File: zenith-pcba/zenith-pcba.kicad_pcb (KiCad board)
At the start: 2 copper layers, 20 parts, among them SW1 G4R152312, U1 XC7A50T-CSG325, U2 K4B4G1646E-BCNB, U3 CH347T, U4 AP63203WU, X1 SX5B8.000F1520F30

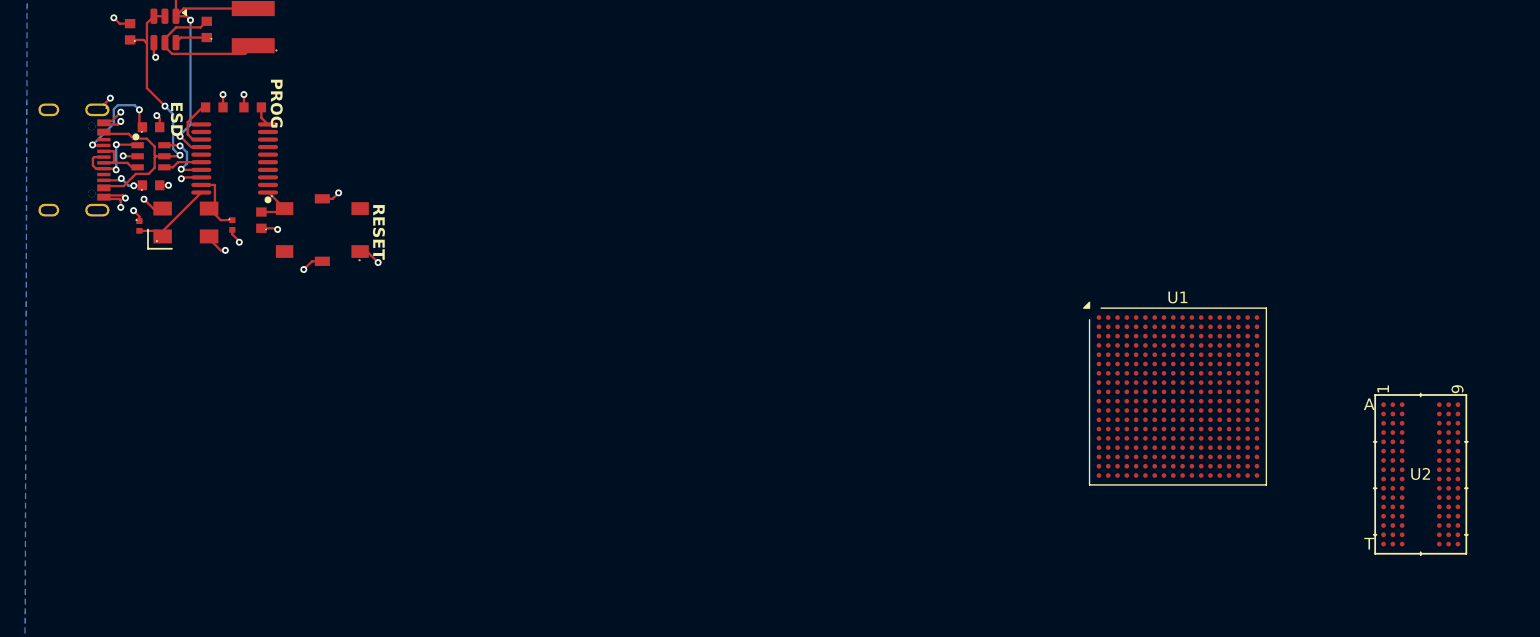
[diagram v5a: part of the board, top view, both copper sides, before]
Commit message: chore(pcba): import din connectors
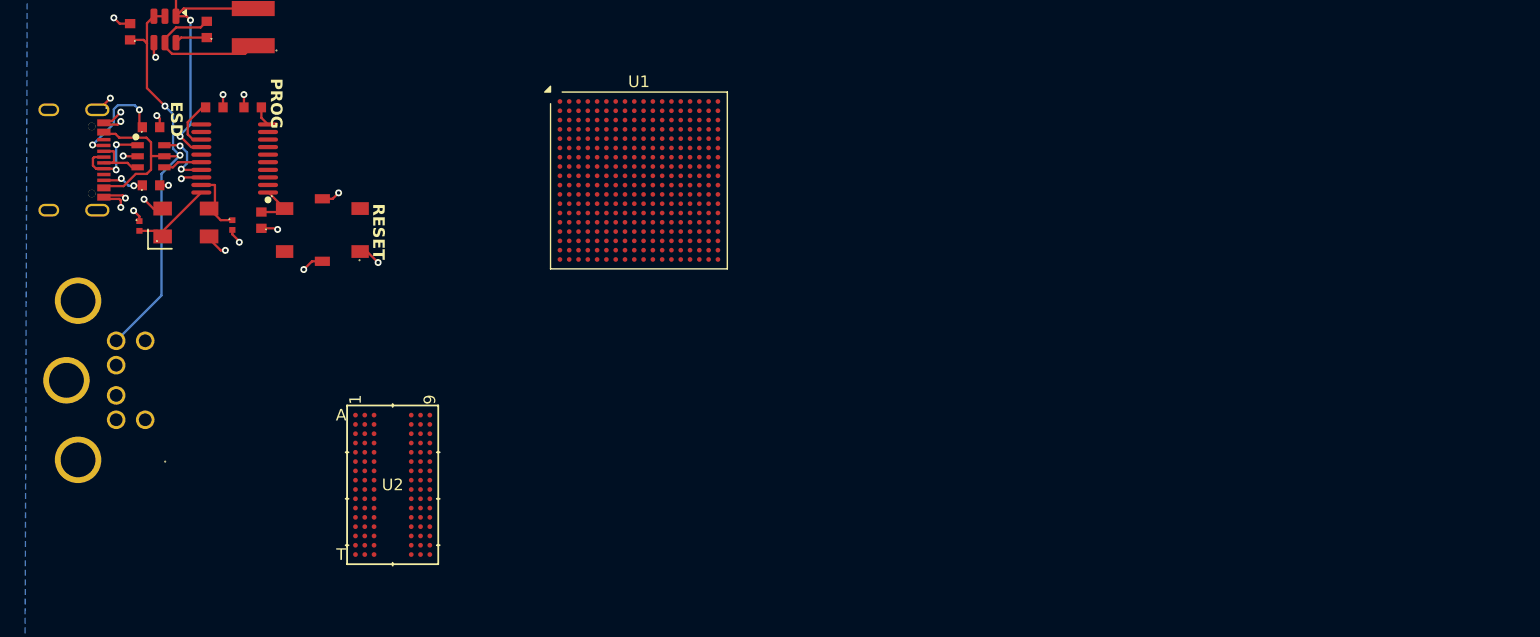
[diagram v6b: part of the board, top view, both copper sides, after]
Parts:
- added PS1: DS1093-01-PN60, easyeda2kicad:CONN-TH_DS1093-01-PN60, F.Cu at (64.1, 85.4)
- moved U2 88.5 mm to (88.8, 94.4)
- moved U1 50.0 mm to (110.0, 68.2)
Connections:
- net /Programmer/VBUSin renamed VCC5.0
- U1 pad E10: unconnected-(U1E-VCCO_0-PadE10) -> VCC3.3
- U1 pad E11: unconnected-(U1F-VCCBATT_0-PadE11) -> VCC1.8
- U1 pad F11: unconnected-(U1F-VCCBRAM-PadF11) -> VCC1.0
- U1 pad F7: unconnected-(U1F-VCCINT-PadF7) -> VCC1.0
- U1 pad F9: unconnected-(U1F-VCCINT-PadF9) -> VCC1.0
- U1 pad G10: unconnected-(U1F-VCCBRAM-PadG10) -> VCC1.0
- U1 pad G12: unconnected-(U1F-VCCAUX-PadG12) -> VCC1.8
- U1 pad G8: unconnected-(U1F-VCCINT-PadG8) -> VCC1.0
- U1 pad H11: unconnected-(U1F-VCCBRAM-PadH11) -> VCC1.0
- U1 pad H13: unconnected-(U1F-VCCAUX-PadH13) -> VCC1.8
- U1 pad H7: unconnected-(U1F-VCCINT-PadH7) -> VCC1.0
- U1 pad H9: unconnected-(U1F-VCCINT-PadH9) -> VCC1.0
- U1 pad J10: unconnected-(U1F-VCCADC_0-PadJ10) -> VCC1.8
- U1 pad J12: unconnected-(U1F-VCCINT-PadJ12) -> VCC1.0
- U1 pad J8: unconnected-(U1F-VCCINT-PadJ8) -> VCC1.0
- U1 pad J9: unconnected-(U1F-GNDADC_0-PadJ9) -> GND
- U1 pad K10: unconnected-(U1E-VP_0-PadK10) -> GND
- U1 pad K11: unconnected-(U1F-VCCINT-PadK11) -> VCC1.0
- U1 pad K13: unconnected-(U1F-VCCAUX-PadK13) -> VCC1.8
- U1 pad K7: unconnected-(U1F-VCCINT-PadK7) -> VCC1.0
- U1 pad K9: unconnected-(U1E-VREFN_0-PadK9) -> GND
- U1 pad L10: unconnected-(U1E-VREFP_0-PadL10) -> GND
- U1 pad L12: unconnected-(U1F-VCCINT-PadL12) -> VCC1.0
- U1 pad L6: unconnected-(U1B-VCCO_34-PadL6) -> VCC3.3
- U1 pad L8: unconnected-(U1F-VCCINT-PadL8) -> VCC1.0
- U1 pad L9: unconnected-(U1E-VN_0-PadL9) -> GND
- U1 pad M11: unconnected-(U1F-VCCINT-PadM11) -> VCC1.0
- U1 pad M13: unconnected-(U1F-VCCAUX-PadM13) -> VCC1.8
- U1 pad M3: unconnected-(U1B-VCCO_34-PadM3) -> VCC3.3
- U1 pad M7: unconnected-(U1F-VCCINT-PadM7) -> VCC1.0
- U1 pad N10: unconnected-(U1F-VCCINT-PadN10) -> VCC1.0
- U1 pad N12: unconnected-(U1F-VCCINT-PadN12) -> VCC1.0
- U1 pad N8: unconnected-(U1F-VCCINT-PadN8) -> VCC1.0
- U1 pad P11: unconnected-(U1F-VCCINT-PadP11) -> VCC1.0
- U1 pad P13: unconnected-(U1F-VCCAUX-PadP13) -> VCC1.8
- U1 pad P7: unconnected-(U1B-VCCO_34-PadP7) -> VCC3.3
- U1 pad P9: unconnected-(U1F-VCCINT-PadP9) -> VCC1.0
- U1 pad R10: unconnected-(U1E-VCCO_0-PadR10) -> VCC3.3
- U1 pad R4: unconnected-(U1B-VCCO_34-PadR4) -> VCC3.3
- U1 pad T1: unconnected-(U1B-VCCO_34-PadT1) -> VCC3.3
- U1 pad V5: unconnected-(U1B-VCCO_34-PadV5) -> VCC3.3
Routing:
- net VCC5.0: track 30.3 -> 48.1 mm

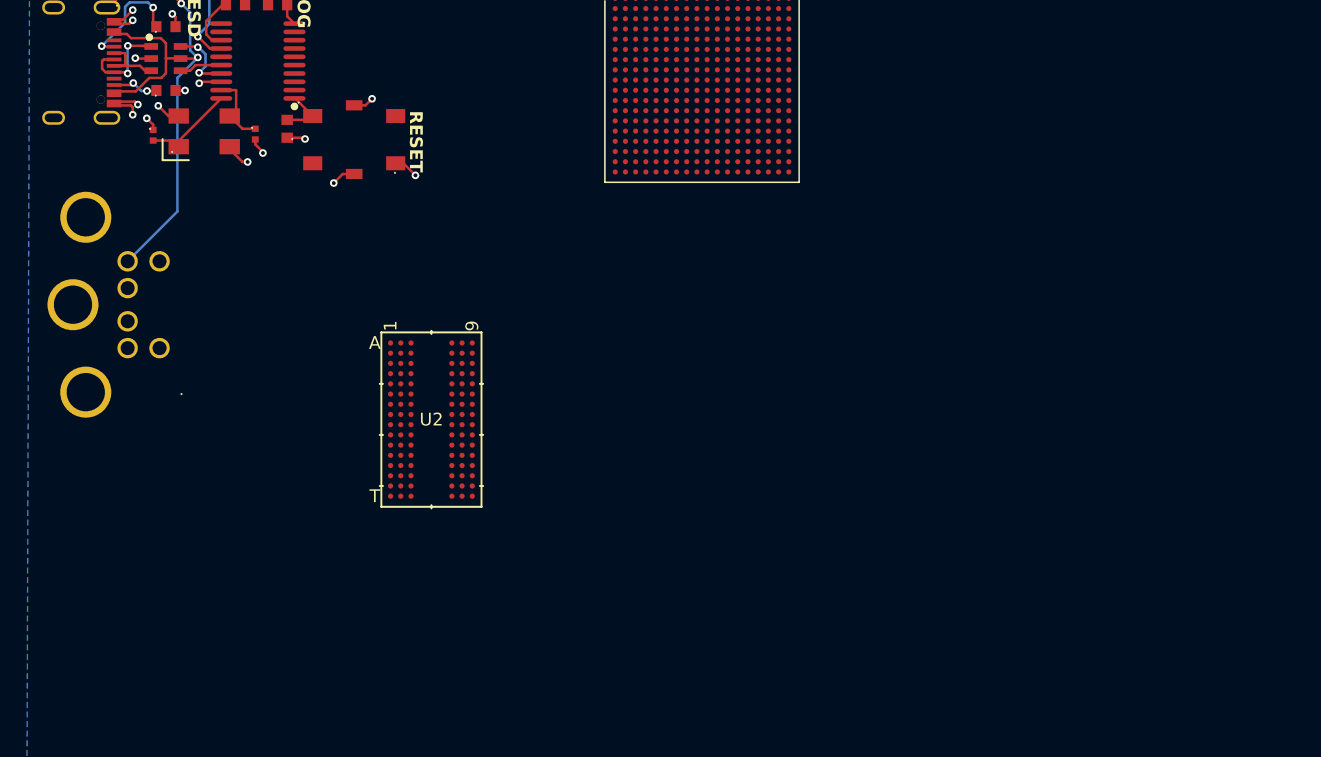
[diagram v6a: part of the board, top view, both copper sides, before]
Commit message: feat(pcba): din esd
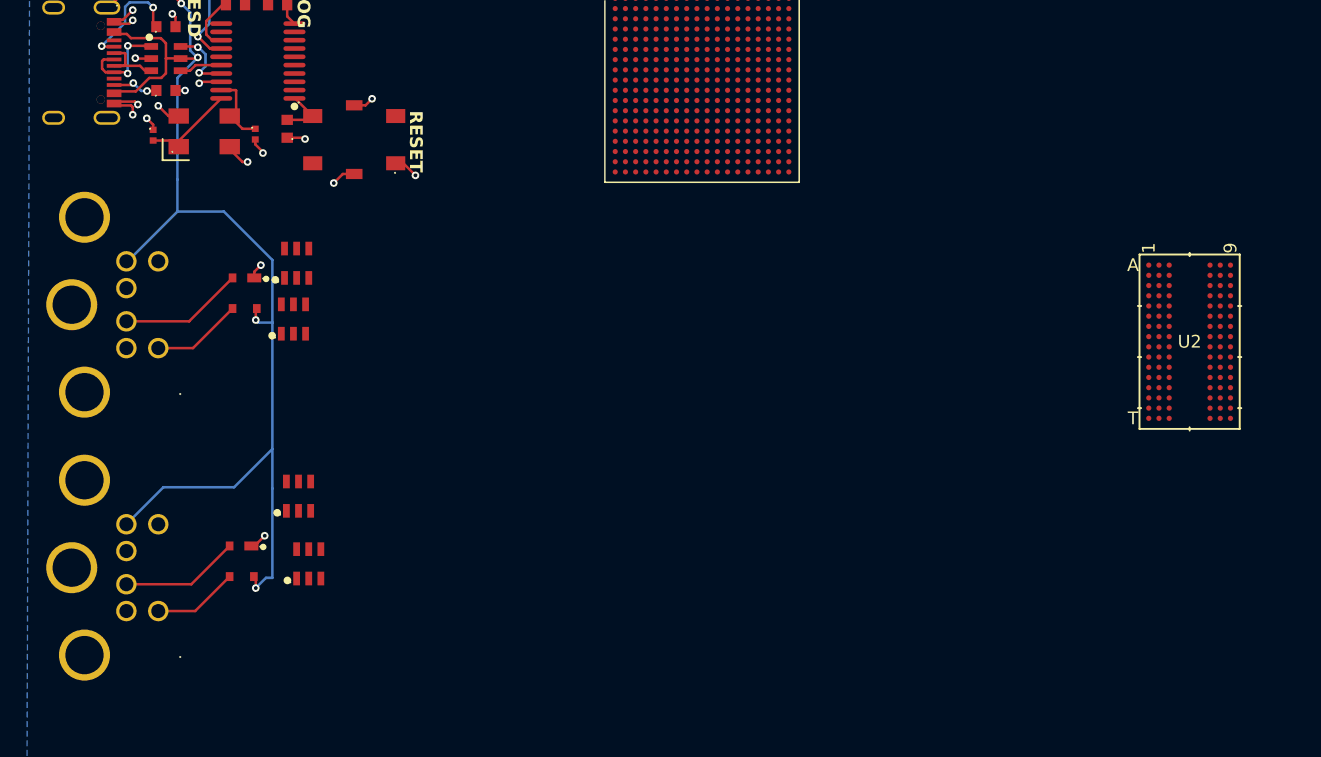
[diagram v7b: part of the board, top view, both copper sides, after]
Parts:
- added D2: PRTR5V0U2X_C5158049, easyeda2kicad:SOT-143_L2.9-W1.3-P1.92-LS2.3-BL, F.Cu at (74.2, 84.5)
- added D3: PRTR5V0U2X_C5158049, easyeda2kicad:SOT-143_L2.9-W1.3-P1.92-LS2.3-BL, F.Cu at (73.9, 105.5)
- added PS2: DS1093-01-PN60, easyeda2kicad:CONN-TH_DS1093-01-PN60, F.Cu at (64.0, 106.0)
- added U5: TXS0101DB, easyeda2kicad:SOT-23-6_L2.9-W1.6-P0.95-LS2.9-BL, F.Cu at (78.2, 82.2)
- added U6: TXS0101DB, easyeda2kicad:SOT-23-6_L2.9-W1.6-P0.95-LS2.9-BL, F.Cu at (78.0, 86.5)
- added U7: TXS0101DB, easyeda2kicad:SOT-23-6_L2.9-W1.6-P0.95-LS2.9-BL, F.Cu at (78.4, 100.4)
- added U8: TXS0101DB, easyeda2kicad:SOT-23-6_L2.9-W1.6-P0.95-LS2.9-BL, F.Cu at (79.2, 105.7)
- moved U2 59.7 mm to (148.2, 88.3)
- moved PS1 0.10 mm to (64.0, 85.4)
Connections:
- PS1 pad 1: unconnected-(PS1-PIN1-Pad1) -> Net-(PS1-PIN1)
- PS1 pad 5: unconnected-(PS1-PIN5-Pad5) -> Net-(PS1-PIN5)
- U1 pad J4: unconnected-(U1B-IO_L2N_T0_34-PadJ4) -> Net-(U1B-IO_L2N_T0_34)
- U1 pad J5: unconnected-(U1B-IO_L2P_T0_34-PadJ5) -> Net-(U1B-IO_L2P_T0_34)
- U1 pad K1: unconnected-(U1B-IO_L3N_T0_DQS_34-PadK1) -> Net-(U1B-IO_L3N_T0_DQS_34)
- U1 pad K2: unconnected-(U1B-IO_L3P_T0_DQS_34-PadK2) -> Net-(U1B-IO_L3P_T0_DQS_34)
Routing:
- net VCC5.0: track 48.1 -> 100.8 mm, vias 2 -> 4
- net Net-(PS1-PIN1): track 0.00 -> 9.73 mm
- net Net-(PS2-PIN1): track 0.00 -> 9.33 mm
- net Net-(PS1-PIN5): track 0.00 -> 7.32 mm
- net Net-(PS2-PIN5): track 0.00 -> 6.76 mm
- net GND: track 34.3 -> 36.6 mm, vias 22 -> 24

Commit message: fix(pcba): route ps2 esd
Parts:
- moved U2 35.1 mm to (125.4, 61.6)
- moved U8 6.89 mm to (73.8, 110.0)
- moved U5 4.58 mm to (74.2, 80.0), turned to 180 degrees
- moved U7 4.55 mm to (74.0, 101.6), turned to 180 degrees
- moved U6 4.41 mm to (74.0, 88.4), turned to 90 degrees
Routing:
- net VCC3.3: track 24.4 -> 99.6 mm, vias 2 -> 6
- net VCC5.0: track 100.8 -> 114.3 mm, vias 4 -> 8
- net GND: track 36.6 -> 43.5 mm, vias 24 -> 28
- net Net-(PS2-PIN5): track 6.76 -> 9.67 mm
- net Net-(PS1-PIN1): track 9.73 -> 11.9 mm
- net Net-(PS1-PIN5): track 7.32 -> 9.23 mm
- net Net-(PS2-PIN1): track 9.33 -> 10.9 mm
